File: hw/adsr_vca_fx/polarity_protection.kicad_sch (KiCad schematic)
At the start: 6 parts, among them Q1 HX2301A

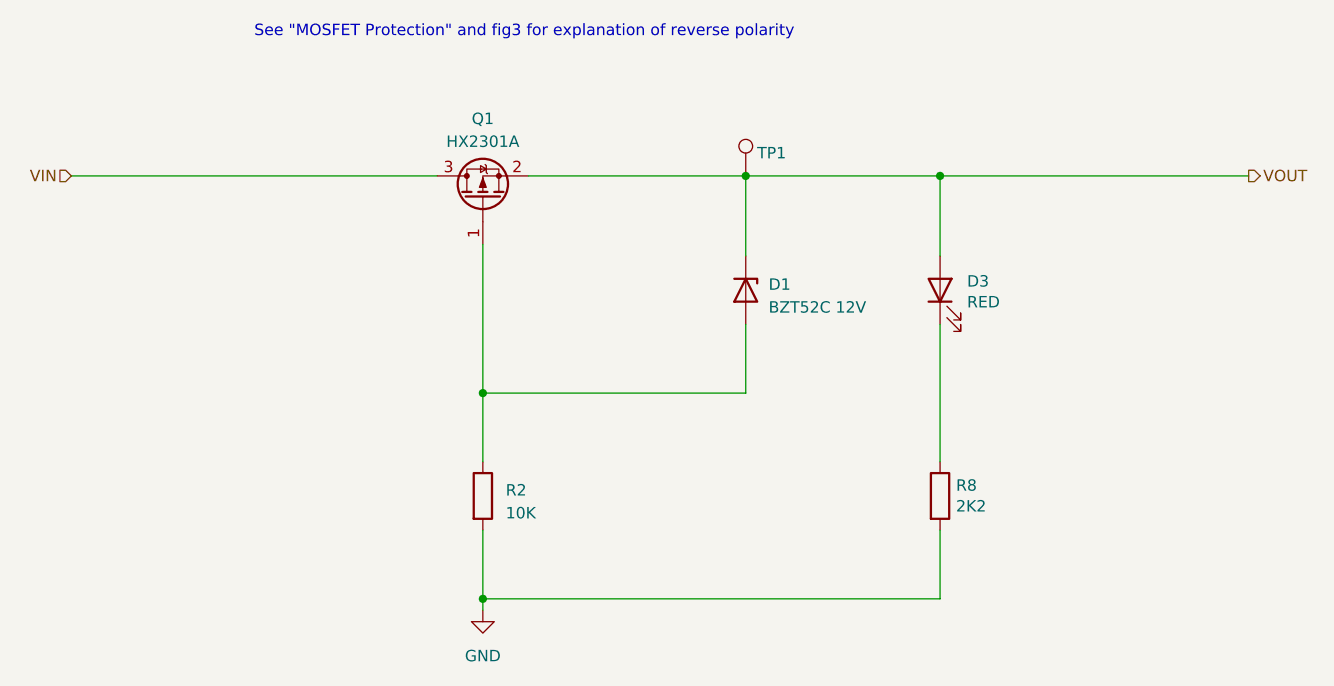
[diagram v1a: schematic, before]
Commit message: updated layout
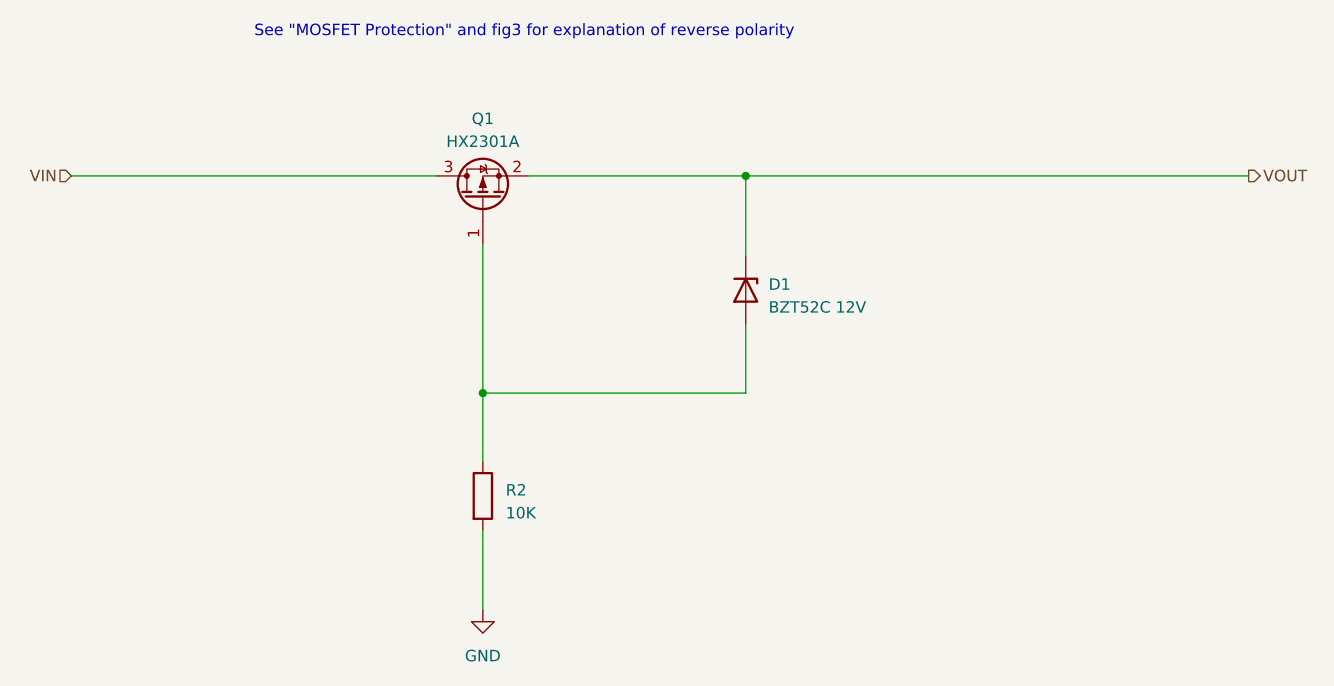
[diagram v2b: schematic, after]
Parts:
- removed D3: RED, LED_SMD:LED_0805_2012Metric_Pad1.15x1.40mm_HandSolder, symbol Device:LED
- removed R8: 2K2, Resistor_SMD:R_0805_2012Metric_Pad1.20x1.40mm_HandSolder, symbol Device:R
- removed TP1: TestPoint, TestPoint:TestPoint_Pad_1.0x1.0mm, symbol Connector:TestPoint
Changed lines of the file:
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@@
   (junction (at 157.48 73.66) (diameter 0) (color 0 0 0 0)
-  )
-  (junction (at 179.07 73.66) (diameter 0) (color 0 0 0 0)
-  )
-  (junction (at 128.27 120.65) (diameter 0) (color 0 0 0 0)
   )
   (wire (pts (xy 128.27 97.79) (xy 128.27 105.41))
@@
     (stroke (width 0) (type default))
   )
-  (wire (pts (xy 128.27 113.03) (xy 128.27 120.65))
-    (stroke (width 0) (type default))
-  )
-  (wire (pts (xy 157.48 73.66) (xy 179.07 73.66))
+  (wire (pts (xy 128.27 113.03) (xy 128.27 121.92))
     (stroke (width 0) (type default))
   )
@@
     (stroke (width 0) (type default))
   )
-  (wire (pts (xy 179.07 73.66) (xy 179.07 82.55))
-    (stroke (width 0) (type default))
-  )
-  (wire (pts (xy 179.07 73.66) (xy 213.36 73.66))
-    (stroke (width 0) (type default))
-  )
-  (wire (pts (xy 179.07 120.65) (xy 128.27 120.65))
+  (wire (pts (xy 157.48 73.66) (xy 213.36 73.66))
     (stroke (width 0) (type default))
   )
@@
     (stroke (width 0) (type default))
   )
-  (wire (pts (xy 179.07 113.03) (xy 179.07 120.65))
-    (stroke (width 0) (type default))
-  )
-  (wire (pts (xy 128.27 120.65) (xy 128.27 121.92))
-    (stroke (width 0) (type default))
-  )
-  (wire (pts (xy 179.07 90.17) (xy 179.07 105.41))
-    (stroke (width 0) (type default))
-  )
   (text "See \"MOSFET Protection\" and fig3 for explanation of reverse polarity"
     (at 102.87 58.42 0)
@@
   (hierarchical_label "VIN" (shape input) (at 82.55 73.66 180) (fields_autoplaced)
     (effects (font (size 1.27 1.27)) (justify right))
-  )
-  (symbol (lib_id "Device:R") (at 179.07 109.22 0) (unit 1)
-    (in_bom yes) (on_board yes) (dnp no)
-    (property "Reference" "R8" (at 180.848 108.0516 0)
-      (effects (font (size 1.27 1.27)) (justify left))
-    )
-    (property "Value" "2K2" (at 180.848 110.363 0)
-      (effects (font (size 1.27 1.27)) (justify left))
-    )
-    (property "Footprint" "Resistor_SMD:R_0805_2012Metric_Pad1.20x1.40mm_HandSolder" (at 177.292 109.22 90)
-      (effects (font (size 1.27 1.27)) hide)
-    )
-    (property "Datasheet" "~" (at 179.07 109.22 0)
-      (effects (font (size 1.27 1.27)) hide)
-    )
-    (property "LcscNo" "~" (at 179.07 109.22 0)
-      (effects (font (size 1.27 1.27)) hide)
-    )
-    (property "Type" "~" (at 179.07 109.22 0)
-      (effects (font (size 1.27 1.27)) hide)
-    )
-    (pin "1")
-    (pin "2")
-    (instances
-      (project "adsr_vca_fx"
-        (path "/2c7cc946-dcca-4ffb-b6a0-bf0c9ddb491b/d2509004-b5c4-4b3c-af62-d7c90bd19790/cfda1149-d0fd-45bd-b9f5-d59eb44c2b04"
-          (reference "R8") (unit 1)
-        )
-        (path "/2c7cc946-dcca-4ffb-b6a0-bf0c9ddb491b/d2509004-b5c4-4b3c-af62-d7c90bd19790/7f56a6d0-e9ac-40b5-a9da-5532f531790a"
-          (reference "R26") (unit 1)
-        )
-      )
-    )
   )
   (symbol (lib_id "Device:Q_PMOS_GSD") (at 128.27 76.2 90) (unit 1)
@@
         (path "/2c7cc946-dcca-4ffb-b6a0-bf0c9ddb491b/d2509004-b5c4-4b3c-af62-d7c90bd19790/7f56a6d0-e9ac-40b5-a9da-5532f531790a"
           (reference "Q1") (unit 1)
-        )
-      )
-    )
-  )
-  (symbol (lib_id "Device:LED") (at 179.07 86.36 90) (unit 1)
-    (in_bom yes) (on_board yes) (dnp no)
-    (property "Reference" "D3" (at 182.0672 85.3694 90)
-      (effects (font (size 1.27 1.27)) (justify right))
-    )
-    (property "Value" "RED" (at 182.0672 87.6808 90)
-      (effects (font (size 1.27 1.27)) (justify right))
-    )
-    (property "Footprint" "LED_SMD:LED_0805_2012Metric_Pad1.15x1.40mm_HandSolder" (at 179.07 86.36 0)
-      (effects (font (size 1.27 1.27)) hide)
-    )
-    (property "Datasheet" "~" (at 179.07 86.36 0)
-      (effects (font (size 1.27 1.27)) hide)
-    )
-    (property "LcscNo" "C2293" (at 179.07 86.36 0)
-      (effects (font (size 1.27 1.27)) hide)
-    )
-    (property "Type" "~" (at 179.07 86.36 0)
-      (effects (font (size 1.27 1.27)) hide)
-    )
-    (pin "1")
-    (pin "2")
-    (instances
-      (project "adsr_vca_fx"
-        (path "/2c7cc946-dcca-4ffb-b6a0-bf0c9ddb491b/d2509004-b5c4-4b3c-af62-d7c90bd19790/cfda1149-d0fd-45bd-b9f5-d59eb44c2b04"
-          (reference "D3") (unit 1)
-        )
-        (path "/2c7cc946-dcca-4ffb-b6a0-bf0c9ddb491b/d2509004-b5c4-4b3c-af62-d7c90bd19790/7f56a6d0-e9ac-40b5-a9da-5532f531790a"
-          (reference "D4") (unit 1)
         )
       )
@@
         )
       )
-    )
-  )
-  (symbol (lib_id "Connector:TestPoint") (at 157.48 73.66 0) (unit 1)
-    (in_bom yes) (on_board yes) (dnp no)
-    (property "Reference" "TP1" (at 158.75 71.12 0)
-      (effects (font (size 1.27 1.27)) (justify left))
-    )
-    (property "Value" "TestPoint" (at 160.02 72.263 0)
-      (effects (font (size 1.27 1.27)) (justify left) hide)
-    )
-    (property "Footprint" "TestPoint:TestPoint_Pad_1.0x1.0mm" (at 162.56 73.66 0)
-      (effects (font (size 1.27 1.27)) hide)
-    )
-    (property "Datasheet" "~" (at 162.56 73.66 0)
-      (effects (font (size 1.27 1.27)) hide)
-    )
-    (pin "1")
-    (instances
-      (project "adsr_vca_fx"
-        (path "/2c7cc946-dcca-4ffb-b6a0-bf0c9ddb491b/0d7fbd8f-e081-47cd-87b5-dfbc75ed6757"
-          (reference "TP1") (unit 1)
-        )
-        (path "/2c7cc946-dcca-4ffb-b6a0-bf0c9ddb491b/d2509004-b5c4-4b3c-af62-d7c90bd19790"
-          (reference "TP5") (unit 1)
-        )
-        (path "/2c7cc946-dcca-4ffb-b6a0-bf0c9ddb491b/d2509004-b5c4-4b3c-af62-d7c90bd19790/7f56a6d0-e9ac-40b5-a9da-5532f531790a"
-          (reference "TP10") (unit 1)
-        )
-      )
